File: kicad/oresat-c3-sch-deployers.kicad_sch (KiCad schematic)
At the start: 26 parts, among them Q10 FDMQ86530L, Q11 DMP2240UDM-7, Q5 DMP2240UDM-7, Q7 DMP2240UDM-7, Q8 FDMQ86530L, Q9 DMP2240UDM-7

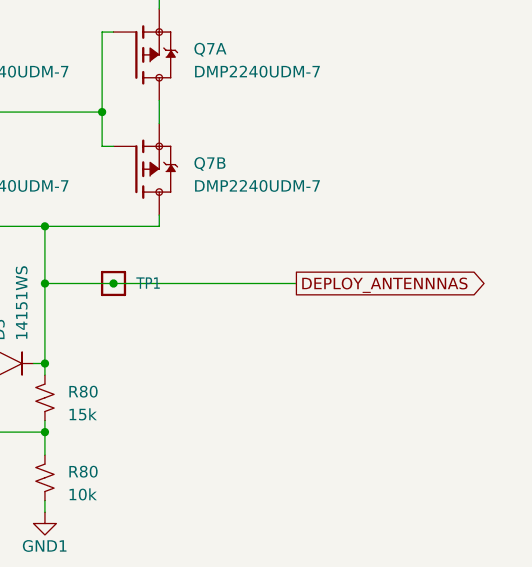
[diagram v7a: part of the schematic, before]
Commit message: More progress on C3 v6. All ICs and Packages are in, deployer and power supply and I2C subsystems laid out.
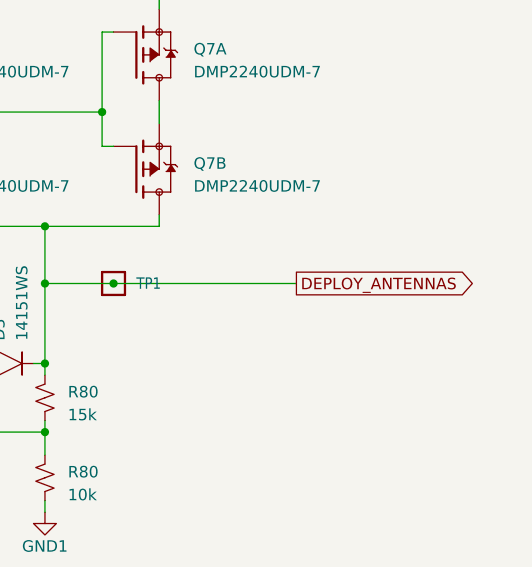
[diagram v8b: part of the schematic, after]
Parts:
- Q11, Q5, Q7, Q9: footprint oresat-footprints:SOT23-6 -> Package_TO_SOT_SMD:SOT-23-6
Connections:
- net DEPLOY_ANTENNNAS renamed DEPLOY_ANTENNAS
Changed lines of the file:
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@@
     )
   )
-  (global_label "DEPLOY_ANTENNNAS" (shape output) (at 288.29 73.66 0) (fields_autoplaced)
+  (global_label "DEPLOY_ANTENNAS" (shape output) (at 288.29 73.66 0) (fields_autoplaced)
     (effects (font (size 1.27 1.27)) (justify left))
-    (property "Intersheetrefs" "${INTERSHEET_REFS}" (at 310.1249 73.66 0)
+    (property "Intersheetrefs" "${INTERSHEET_REFS}" (at 308.7944 73.66 0)
       (effects (font (size 1.27 1.27)) (justify left))
     )
@@
       (effects (font (size 1.27 1.27)) (justify left))
     )
-    (property "Footprint" "oresat-footprints:SOT23-6" (at 270.51 160.02 0)
+    (property "Footprint" "Package_TO_SOT_SMD:SOT-23-6" (at 270.51 160.02 0)
       (effects (font (size 1.27 1.27)) hide)
     )
@@
       (effects (font (size 1.27 1.27)) (justify left))
     )
-    (property "Footprint" "oresat-footprints:SOT23-6" (at 242.57 172.72 0)
+    (property "Footprint" "Package_TO_SOT_SMD:SOT-23-6" (at 242.57 172.72 0)
       (effects (font (size 1.27 1.27)) hide)
     )
@@
       (effects (font (size 1.27 1.27)) (justify left))
     )
-    (property "Footprint" "oresat-footprints:SOT23-6" (at 270.51 46.99 0)
+    (property "Footprint" "Package_TO_SOT_SMD:SOT-23-6" (at 270.51 46.99 0)
       (effects (font (size 1.27 1.27)) hide)
     )
@@
       (effects (font (size 1.27 1.27)) (justify left))
     )
-    (property "Footprint" "oresat-footprints:SOT23-6" (at 242.57 46.99 0)
+    (property "Footprint" "Package_TO_SOT_SMD:SOT-23-6" (at 242.57 46.99 0)
       (effects (font (size 1.27 1.27)) hide)
     )
@@
       (effects (font (size 1.27 1.27)) (justify left))
     )
-    (property "Footprint" "oresat-footprints:SOT23-6" (at 270.51 172.72 0)
+    (property "Footprint" "Package_TO_SOT_SMD:SOT-23-6" (at 270.51 172.72 0)
       (effects (font (size 1.27 1.27)) hide)
     )
@@
       (effects (font (size 1.27 1.27)) (justify left))
     )
-    (property "Footprint" "oresat-footprints:SOT23-6" (at 242.57 160.02 0)
+    (property "Footprint" "Package_TO_SOT_SMD:SOT-23-6" (at 242.57 160.02 0)
       (effects (font (size 1.27 1.27)) hide)
     )
@@
       (effects (font (size 1.27 1.27)) (justify left))
     )
-    (property "Footprint" "oresat-footprints:SOT23-6" (at 270.51 34.29 0)
+    (property "Footprint" "Package_TO_SOT_SMD:SOT-23-6" (at 270.51 34.29 0)
       (effects (font (size 1.27 1.27)) hide)
     )
@@
       (effects (font (size 1.27 1.27)) (justify left))
     )
-    (property "Footprint" "oresat-footprints:SOT23-6" (at 242.57 34.29 0)
-      (effects (font (size 1.27 1.27)) hide)
-    )
+    (property "Footprint" "Package_TO_SOT_SMD:SOT-23-6" (at 242.57 34.29 0)
+      (effects (font (size 1.27 1.27)) hide)
+    )
